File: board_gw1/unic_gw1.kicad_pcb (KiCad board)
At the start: 4 copper layers, 49.5 x 15.2 mm, 109 parts, among them Q1 2N7002, Q10 2N7002, Q11 2N7002, Q12 2N7002, Q13 2N7002, Q14 2N7002, Q15 2N7002, Q16 2N7002, Q17 2N7002, Q18 2N7002, Q19 2N7002, Q2 2N7002, Q20 2N7002, Q21 2N7002, Q22 2N7002, Q23 2N7002, Q24 2N7002, Q25 2N7002, Q26 2N7002, Q27 2N7002, Q28 2N7002, Q29 2N7002, Q3 2N7002, Q30 2N7002, Q31 2N7002, Q32 2N7002, Q33 2N7002, Q34 2N7002, Q35 2N7002, Q36 2N7002, Q37 2N7002, Q38 2N7002, Q39 2N7002, Q4 2N7002, Q40 2N7002, Q5 2N7002, Q6 2N7002, Q7 2N7002, Q8 2N7002, Q9 2N7002, U1 GW1N-LV9QN88C6_I5_, U2 LM3480-3.3, U3 LM3480-5.0, U4 ESP-PSRAM32, U5 AT25SF081-XMHF-X, U6 AP62150Z6, X1 ASE-xxxMHz

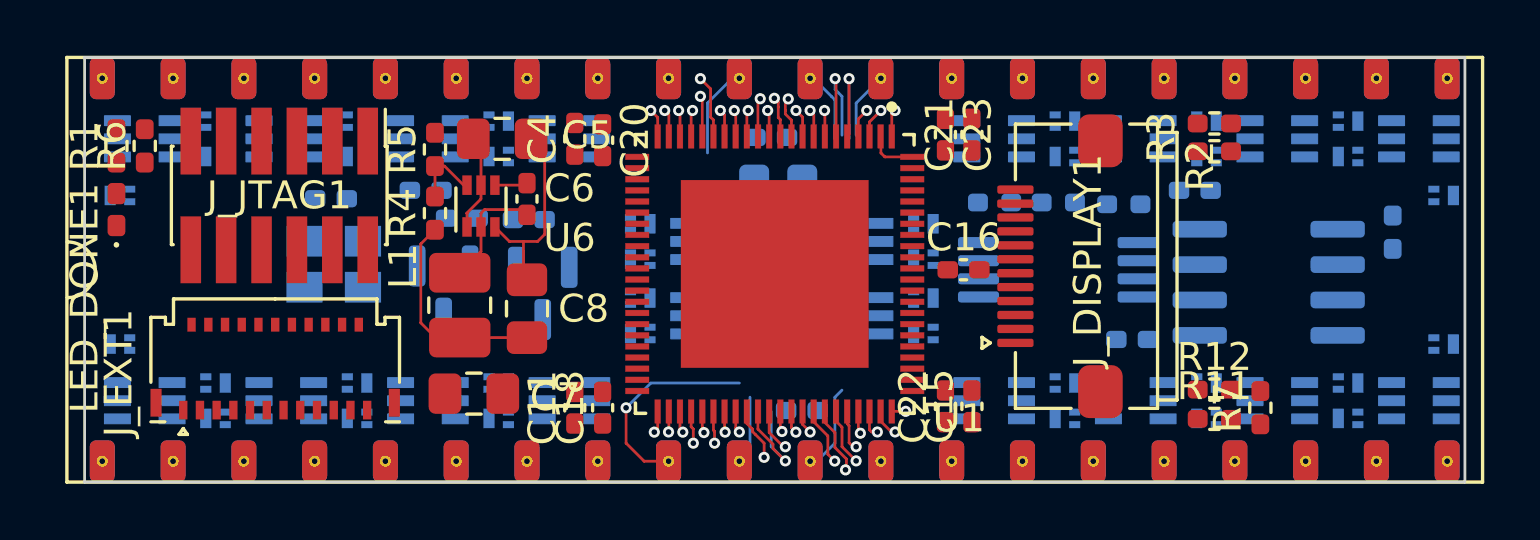
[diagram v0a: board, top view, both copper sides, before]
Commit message: Added extra diodes to shunt ESD path.
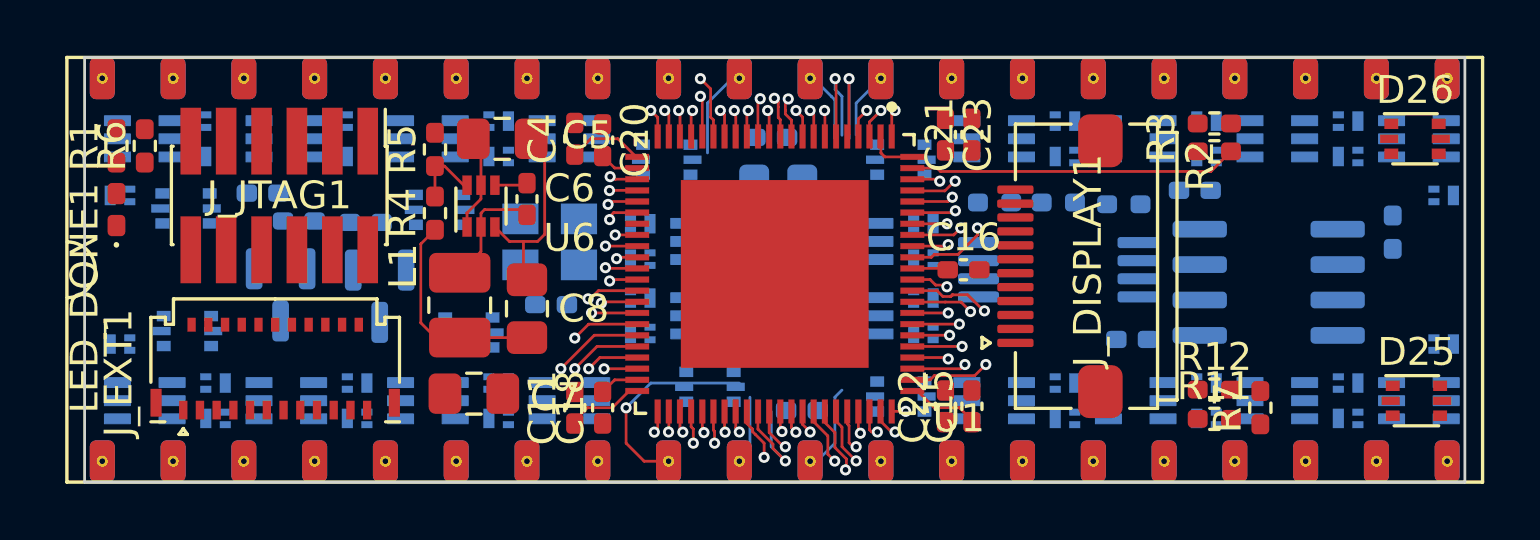
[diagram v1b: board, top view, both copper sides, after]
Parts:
- added D21: BAT54CV, Package_TO_SOT_SMD:SOT-666, B.Cu at (128.2, 97.5)
- added D22: BAT54CV, Package_TO_SOT_SMD:SOT-666, B.Cu at (138.2, 97.5)
- added D23: BAT54CV, Package_TO_SOT_SMD:SOT-666, B.Cu at (146.9, 99.5)
- added D24: BAT54CV, Package_TO_SOT_SMD:SOT-666, B.Cu at (153.8, 99.8)
- added D25: BAT54CV, Package_TO_SOT_SMD:SOT-666, F.Cu at (172.2, 100.0)
- added D26: BAT54CV, Package_TO_SOT_SMD:SOT-666, F.Cu at (172.2, 90.5)
- added D27: BAT54CV, Package_TO_SOT_SMD:SOT-666, B.Cu at (153.8, 91.3)
- added D28: BAT54CV, Package_TO_SOT_SMD:SOT-666, B.Cu at (145.3, 91.3)
- added D29: BAT54CV, Package_TO_SOT_SMD:SOT-666, B.Cu at (137.2, 93.1)
- added D30: BAT54CV, Package_TO_SOT_SMD:SOT-666, B.Cu at (128.1, 93.0)
- moved C17 8.77 mm to (141.2, 96.5)
- moved X1 7.79 mm to (141.2, 94.2)
- moved U3 5.85 mm to (135.1, 96.2)
- moved C1 5.85 mm to (134.6, 93.5)
- moved C2 5.85 mm to (130.8, 92.5)
- moved C3 5.85 mm to (132.2, 93.5)
- moved U2 5.85 mm to (131.5, 96.2)
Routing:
- net Net-(R2-Pad2): track 0.00 -> 11.8 mm
- net +3V3: track 2.77 -> 12.2 mm
- net /PIN2_F: track 0.00 -> 3.24 mm, vias 0 -> 1
- net /PIN20_F: track 0.00 -> 3.01 mm, vias 0 -> 1
- net /PIN22_F: track 0.00 -> 2.92 mm, vias 0 -> 1
- net /PIN12_F: track 0.00 -> 2.87 mm, vias 0 -> 1
- net GND: track 11.7 -> 14.6 mm
- net /PIN3_F: track 0.00 -> 2.64 mm, vias 0 -> 1
- net /PIN1_F: track 0.00 -> 2.45 mm, vias 0 -> 1
- net /PIN19_F: track 0.00 -> 2.23 mm, vias 0 -> 1
- net /PIN13_F: track 0.00 -> 1.95 mm, vias 0 -> 1
- net /PIN4_F: track 0.00 -> 1.91 mm, vias 0 -> 1
- net /IO2A: track 0.00 -> 1.89 mm, vias 0 -> 1
- net /PIN24_F: track 0.00 -> 1.84 mm, vias 0 -> 1
- net /PIN15_F: track 0.00 -> 1.79 mm, vias 0 -> 1
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
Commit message: GW1-based board is fully routed. Cleanup still needed!
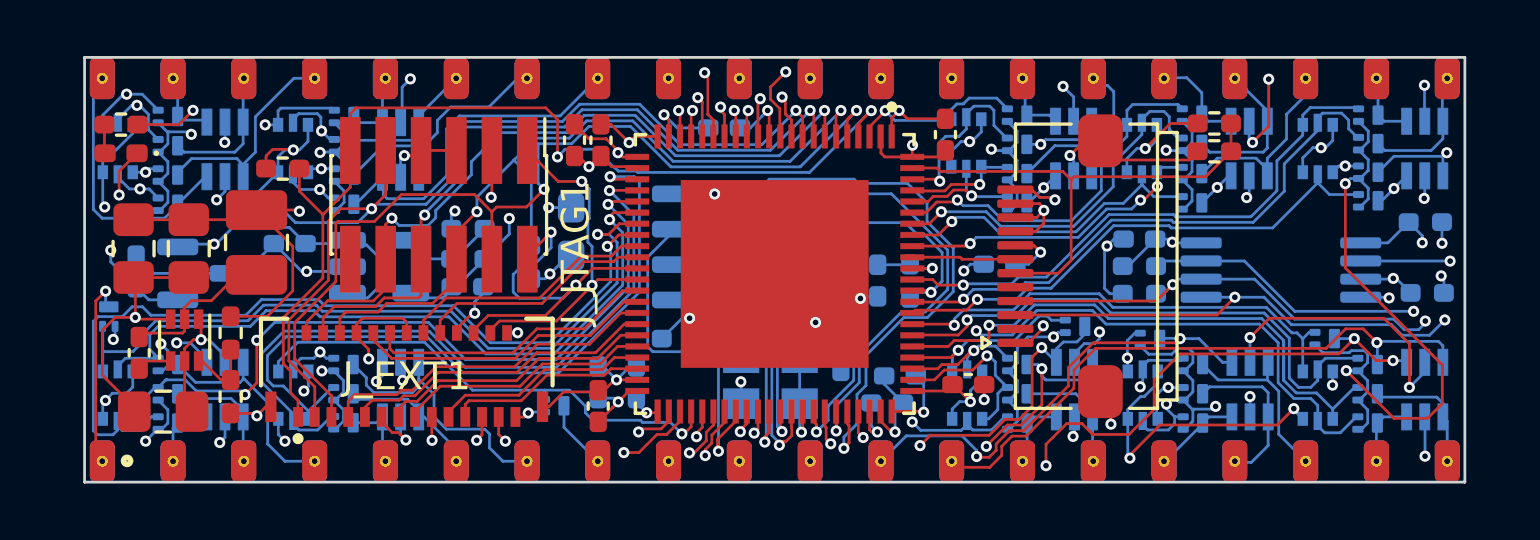
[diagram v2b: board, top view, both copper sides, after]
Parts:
- removed D10, D12, D13, D14, D15, D16, D17, D18, D19, D20: BAT54SDW-7-F, UNIC:SOT65P210X110-6N
- added R14: 4.99k, Resistor_SMD:R_0402_1005Metric_Pad0.72x0.64mm_HandSolder, B.Cu at (138.2, 94.9)
- added R15: 10k, Resistor_SMD:R_0402_1005Metric_Pad0.72x0.64mm_HandSolder, B.Cu at (138.2, 93.8)
- added R16: 10k, Resistor_SMD:R_0402_1005Metric_Pad0.72x0.64mm_HandSolder, F.Cu at (131.6, 91.6)
- C16, C18, C21, C22, D25, D26, R6, R7: moved to B.Cu
- C3: value 0.1u -> 2.2u
- D1, D11, D2, D3, D4, D5, D6, D7, D8, D9: value BAT54SDW-7-F -> BAT54DF
- J_EXT1: value Conn_01x23_MountingPin -> Conn_01x27_MountingPin; footprint UNIC:Molex_502598-2393_2Rows-23Pins-1MP_P0.60mm_Horizontal -> UNIC:Molex_502598-2793_2Rows-23P~0.60mm_Horizontal
- J_JTAG1: footprint Connector_PinHeader_1.27mm:PinHeader_2x06_P1.27mm_Vertical_SMD -> UNIC:PinHeader_2x06_P1.27mm_Vertical_SMD
- Q1, Q10, Q11, Q12, Q13, Q14, Q15, Q16, Q17, Q18, Q19, Q2, Q20, Q21, Q22, Q23, Q24, Q25, Q26, Q27, Q28, Q29, Q3, Q30, Q31, Q32, Q33, Q34, Q35, Q36, Q37, Q38, Q39, Q4, Q40, Q5, Q6, Q7, Q8, Q9: footprint Package_DFN_QFN:Diodes_DFN1006-3 -> UNIC:SOT-883
- R11: value 1k -> 10k; moved to B.Cu
- R12: value DNC -> 10k; moved to B.Cu
- R3: value 1k -> 10k
- U3: value LM3480-5.0 -> AP2202K-ADJ; footprint Package_TO_SOT_SMD:SOT-23 -> Package_TO_SOT_SMD:SOT-23-5
- moved D9 38.8 mm to (129.5, 90.9), turned to -90 degrees
- moved R7 36.7 mm to (130.6, 93.2), turned to 0 degrees
- moved D8 27.9 mm to (135.8, 91.0), turned to -90 degrees
- moved D5 25.7 mm to (172.6, 99.5), turned to -90 degrees
- moved D4 24.4 mm to (166.3, 99.5), turned to -90 degrees
- moved D3 23.2 mm to (160.0, 99.5), turned to -90 degrees
- moved Q11 22.0 mm to (170.5, 89.7)
- moved R12 19.3 mm to (145.8, 97.7), turned to 180 degrees
- moved U4 18.7 mm to (148.3, 94.4), turned to 0 degrees
- moved R13 17.4 mm to (154.1, 95.7), turned to -90 degrees
- moved Q12 17.4 mm to (170.5, 90.7), turned to 0 degrees
- moved C19 16.5 mm to (147.4, 90.2)
- moved Q9 15.6 mm to (160.0, 97.3)
- moved C5 15.6 mm to (127.3, 100.3), turned to 180 degrees
- moved R9 15.5 mm to (172.6, 93.5), turned to 180 degrees
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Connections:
- D1 pad 1: GND -> /PIN1
- D1 pad 3: /PIN1 -> /PIN4
- D1 pad 4: GND -> /PIN3
- D1 pad 5: LINE -> GND
- D11 pad 1: GND -> /PIN22
- D11 pad 4: GND -> /PIN28
- D11 pad 5: LINE -> GND
- D11 pad 6: /PIN22 -> /PIN30
- D2 pad 1: GND -> /PIN8
- D2 pad 3: /PIN3 -> /PIN7
- D2 pad 4: GND -> /PIN6
- D2 pad 5: LINE -> GND
- D2 pad 6: /PIN4 -> /PIN5
- D21 pad 2: /PIN2_F -> /PIN4_F
- D21 pad 5: /PIN4_F -> /PIN2_F
- D22 pad 1: /PIN5_F -> /PIN8_F
- D22 pad 2: /PIN6_F -> /PIN7_F
- D22 pad 4: /PIN7_F -> /PIN6_F
- D22 pad 5: /PIN8_F -> /PIN5_F
- D23 pad 4: /PIN11_F -> /PIN15_F
- D23 pad 5: /PIN12_F -> /PIN14_F
- D24 pad 1: /PIN13_F -> /PIN12_F
- D24 pad 2: /PIN14_F -> /PIN18_F
- D24 pad 4: /PIN15_F -> /PIN17_F
- D25 pad 1: /PIN17_F -> /PIN11_F
- D25 pad 2: /PIN18_F -> /PIN13_F
- D25 pad 4: /PIN19_F -> /PIN20_F
- D25 pad 5: /PIN20_F -> /PIN19_F
- D26 pad 1: /PIN21_F -> /PIN22_F
- D26 pad 2: /PIN22_F -> /PIN21_F
- D26 pad 4: /PIN23_F -> /PIN28_F
- D26 pad 5: /PIN24_F -> /PIN30_F
- D27 pad 2: /PIN26_F -> /PIN24_F
- D27 pad 4: /PIN27_F -> /PIN23_F
- D27 pad 5: /PIN28_F -> /PIN29_F
- D28 pad 1: /PIN29_F -> /PIN27_F
- D28 pad 2: /PIN30_F -> /PIN31_F
- D28 pad 4: /PIN31_F -> /PIN26_F
- D29 pad 1: /PIN33_F -> /PIN36_F
- D29 pad 2: /PIN34_F -> /PIN35_F
- D29 pad 4: /PIN35_F -> /PIN34_F
- D29 pad 5: /PIN36_F -> /PIN33_F
- D3 pad 1: GND -> /PIN9
- D3 pad 3: /PIN5 -> /PIN10
- D3 pad 4: GND -> /PIN15
- D3 pad 5: LINE -> GND
- D3 pad 6: /PIN6 -> /PIN14
- D30 pad 1: /PIN37_F -> /PIN39_F
- D30 pad 4: /PIN39_F -> /PIN37_F
- D4 pad 1: GND -> /PIN12
- D4 pad 3: /PIN7 -> /PIN18
- D4 pad 4: GND -> /PIN17
- D4 pad 5: LINE -> GND
- D4 pad 6: /PIN8 -> /PIN16
- D5 pad 1: GND -> /PIN11
- D5 pad 3: /PIN9 -> /PIN13
- D5 pad 4: GND -> /PIN20
- D5 pad 5: LINE -> GND
- D5 pad 6: /PIN10 -> /PIN19
- D6 pad 1: GND -> /PIN25
- D6 pad 3: /PIN11 -> /PIN24
- D6 pad 4: GND -> /PIN23
- D6 pad 5: LINE -> GND
- D6 pad 6: /PIN12 -> /PIN29
- D7 pad 1: GND -> /PIN27
- D7 pad 3: /PIN13 -> /PIN31
- D7 pad 4: GND -> /PIN26
- D7 pad 5: LINE -> GND
- D7 pad 6: /PIN14 -> /PIN32
- D8 pad 1: GND -> /PIN36
- D8 pad 3: /PIN15 -> /PIN35
- D8 pad 4: GND -> /PIN34
- D8 pad 5: LINE -> GND
- D8 pad 6: /PIN16 -> /PIN33
- D9 pad 1: GND -> /PIN39
- D9 pad 3: /PIN17 -> /PIN38
- D9 pad 4: GND -> /PIN37
- D9 pad 5: LINE -> GND
- D9 pad 6: /PIN18 -> /PIN40
- J_EXT1 pad 1: GND -> /JTAG_SEL_N
- J_EXT1 pad 10: GND -> /IO2A
- J_EXT1 pad 11: /IO4A -> GND
- J_EXT1 pad 12: /IO4B -> /IO2B
- J_EXT1 pad 13: GND -> /IO3A
- J_EXT1 pad 14: /IO5A -> GND
- J_EXT1 pad 15: /IO5B -> /IO3B
- J_EXT1 pad 16: GND -> /IO4A
- J_EXT1 pad 17: /IO6A -> GND
- J_EXT1 pad 18: /IO6B -> /IO4B
- J_EXT1 pad 19: /RECONFIG_N -> /IO5A
- J_EXT1 pad 2: /IO1A -> /JTAG_TDI
- J_EXT1 pad 20: /JTAG_SEL_N -> GND
- J_EXT1 pad 21: +5V -> /IO5B
- J_EXT1 pad 22: +3V3 -> /IO6A
- J_EXT1 pad 23: +3V3 -> GND
- J_EXT1 pad 3: /IO1B -> /RECONFIG_N
- J_EXT1 pad 4: GND -> /JTAG_TDO
- J_EXT1 pad 5: /IO2A -> /JTAG_TMS
- J_EXT1 pad 6: /IO2B -> /JTAG_TCK
- J_EXT1 pad 7: GND -> /IO1A
- J_EXT1 pad 8: /IO3A -> GND
- J_EXT1 pad 9: /IO3B -> /IO1B
- J_JTAG1 pad 1: /SER_RXD -> /IO6B
- J_JTAG1 pad 10: /JTAG_TDO -> /JTAG_TDI
- J_JTAG1 pad 12: /JTAG_RST -> unconnected-(J_JTAG1-Pad12)
- J_JTAG1 pad 2: /SER_TXD -> /IO6A
- Q11 pad 2: /PIN11_F -> /PIN22_F
- Q11 pad 3: /PIN11 -> /PIN22
- Q12 pad 2: /PIN12_F -> /PIN21_F
- Q12 pad 3: /PIN12 -> /PIN21
- Q13 pad 2: /PIN13_F -> /PIN15_F
- Q13 pad 3: /PIN13 -> /PIN15
- Q15 pad 2: /PIN15_F -> /PIN12_F
- Q15 pad 3: /PIN15 -> /PIN12
- Q16 pad 2: /PIN16_F -> /PIN18_F
- Q16 pad 3: /PIN16 -> /PIN18
- Q18 pad 2: /PIN18_F -> /PIN16_F
- Q18 pad 3: /PIN18 -> /PIN16
- Q19 pad 2: /PIN19_F -> /PIN11_F
- Q19 pad 3: /PIN19 -> /PIN11
- Q2 pad 2: /PIN2_F -> /PIN4_F
- Q2 pad 3: /PIN2 -> /PIN4
- Q20 pad 2: /PIN20_F -> /PIN13_F
- Q20 pad 3: /PIN20 -> /PIN13
- Q21 pad 2: /PIN21_F -> /PIN20_F
- Q21 pad 3: /PIN21 -> /PIN20
- Q22 pad 2: /PIN22_F -> /PIN19_F
- Q22 pad 3: /PIN22 -> /PIN19
- Q23 pad 2: /PIN23_F -> /PIN25_F
- Q23 pad 3: /PIN23 -> /PIN25
- Q25 pad 2: /PIN25_F -> /PIN28_F
- Q25 pad 3: /PIN25 -> /PIN28
- Q26 pad 2: /PIN26_F -> /PIN30_F
- Q26 pad 3: /PIN26 -> /PIN30
- Q27 pad 2: /PIN27_F -> /PIN23_F
- Q27 pad 3: /PIN27 -> /PIN23
- Q28 pad 2: /PIN28_F -> /PIN29_F
- Q28 pad 3: /PIN28 -> /PIN29
- Q29 pad 2: /PIN29_F -> /PIN27_F
- Q29 pad 3: /PIN29 -> /PIN27
- Q30 pad 2: /PIN30_F -> /PIN31_F
- Q30 pad 3: /PIN30 -> /PIN31
- Q31 pad 2: /PIN31_F -> /PIN26_F
- Q31 pad 3: /PIN31 -> /PIN26
- Q33 pad 2: /PIN33_F -> /PIN36_F
- Q33 pad 3: /PIN33 -> /PIN36
- Q34 pad 2: /PIN34_F -> /PIN35_F
- Q34 pad 3: /PIN34 -> /PIN35
- Q35 pad 2: /PIN35_F -> /PIN34_F
- Q35 pad 3: /PIN35 -> /PIN34
- Q36 pad 2: /PIN36_F -> /PIN33_F
- Q36 pad 3: /PIN36 -> /PIN33
- Q37 pad 2: /PIN37_F -> /PIN39_F
- Q37 pad 3: /PIN37 -> /PIN39
- Q39 pad 2: /PIN39_F -> /PIN37_F
- Q39 pad 3: /PIN39 -> /PIN37
- Q4 pad 2: /PIN4_F -> /PIN2_F
- Q4 pad 3: /PIN4 -> /PIN2
- Q5 pad 2: /PIN5_F -> /PIN8_F
- Q5 pad 3: /PIN5 -> /PIN8
- Q6 pad 2: /PIN6_F -> /PIN7_F
- Q6 pad 3: /PIN6 -> /PIN7
- Q7 pad 2: /PIN7_F -> /PIN6_F
- Q7 pad 3: /PIN7 -> /PIN6
- Q8 pad 2: /PIN8_F -> /PIN5_F
- Q8 pad 3: /PIN8 -> /PIN5
- R12 pad 1: /PSRAM_CS_N -> Net-(R12-Pad1)
- R2 pad 2: Net-(R2-Pad2) -> /LCD_RST_N
- R3 pad 1: Net-(R2-Pad2) -> /LCD_RST_N
- R7 pad 2: /RECONIFG_N -> /RECONFIG_N
- U1 pad 11: /PIN34_F -> /PIN28_F
- U1 pad 14: /PIN32_F -> /PIN34_F
- U1 pad 15: /PIN31_F -> /PIN35_F
- U1 pad 16: /PIN35_F -> /PIN36_F
- U1 pad 17: /PIN36_F -> /PIN39_F
- U1 pad 18: /PIN37_F -> /PIN38_F
- U1 pad 19: /PIN38_F -> /PIN40_F
- U1 pad 20: /PIN39_F -> /PIN37_F
- U1 pad 25: /IO6B -> /PIN6_F
- U1 pad 26: /IO6A -> /PIN5_F
- U1 pad 27: /PIN40_F -> /PIN3_F
- U1 pad 28: /IO5B -> /PIN4_F
- U1 pad 29: /IO5A -> /PIN1_F
- U1 pad 3: /PIN30_F -> /PIN27_F
- U1 pad 30: /IO4B -> /PIN2_F
- U1 pad 32: /IO3B -> /IO4B
- U1 pad 33: /IO3A -> /IO6A
- U1 pad 34: /IO2B -> /IO6B
- U1 pad 35: /IO2A -> /IO2B
- U1 pad 36: /IO1B -> /IO2A
- U1 pad 38: /PIN1_F -> /IO1B
- U1 pad 39: /PIN2_F -> /IO3A
- U1 pad 40: /PIN3_F -> /IO3B
- U1 pad 41: /PIN4_F -> /IO5A
- U1 pad 42: /PIN5_F -> /IO5B
- U1 pad 47: /PIN6_F -> /PIN7_F
- U1 pad 48: /PIN7_F -> /PIN8_F
- U1 pad 49: /PIN8_F -> /PIN19_F
- U1 pad 50: /PIN9_F -> /PIN12_F
- U1 pad 51: /PIN10_F -> /PIN18_F
- U1 pad 53: /LCD_RST_N -> /PIN17_F
- U1 pad 54: /LCD_CS_N -> /PIN16_F
- U1 pad 57: /PSRAM_CS_N -> Net-(R12-Pad1)
- U1 pad 63: /PIN11_F -> /PIN14_F
- U1 pad 68: /PIN12_F -> /PIN15_F
- U1 pad 69: /PIN13_F -> /PIN10_F
- U1 pad 70: /PIN14_F -> /PIN9_F
- U1 pad 71: /PIN15_F -> /PIN20_F
- U1 pad 72: /PIN16_F -> /PIN13_F
- U1 pad 73: /PIN17_F -> /PIN11_F
- U1 pad 74: /PIN18_F -> /PIN30_F
- U1 pad 75: /PIN19_F -> /PIN21_F
- U1 pad 76: /PIN20_F -> /PSRAM_CS_N
- U1 pad 77: /PIN21_F -> /PIN22_F
- U1 pad 79: /PIN22_F -> /LCD_CS_N
- U1 pad 81: /PIN24_F -> /PIN29_F
- U1 pad 82: /PIN25_F -> /PIN24_F
- U1 pad 83: /PIN26_F -> /PIN25_F
- U1 pad 84: /PIN27_F -> /PIN32_F
- U1 pad 85: /PIN28_F -> /PIN26_F
- U1 pad 86: /PIN29_F -> /PIN31_F
- U1 pad 87: Net-(R2-Pad2) -> /LCD_RST_N
- U1 pad 9: /RECONIFG_N -> /RECONFIG_N
- U3 pad 1: +5V -> LINE
- U3 pad 2: LINE -> GND
- U3 pad 3: GND -> LINE
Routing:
- net +3V3: track 12.2 -> 222.4 mm, vias 3 -> 28
- net GND: track 14.6 -> 221.9 mm, vias 3 -> 38
- net +5V: track 0.00 -> 186.6 mm, vias 0 -> 14
- net LINE: track 3.49 -> 111.9 mm, vias 0 -> 12
- net /SPI_MOSI_IO0: track 2.07 -> 59.4 mm, vias 1 -> 3
- net /SPI_MISO_IO1: track 1.46 -> 56.8 mm, vias 1 -> 2
- net +1V2: track 10.9 -> 63.8 mm, vias 4 -> 5
- net /SPI_CLK: track 2.09 -> 52.9 mm, vias 1 -> 3
- net /SPI_IO3: track 0.74 -> 46.7 mm, vias 1 -> 2
- net /SPI_IO2: track 1.55 -> 46.9 mm, vias 1 -> 2
- net /RECONFIG_N: track 0.00 -> 35.9 mm, vias 0 -> 2
- net /JTAG_SEL_N: track 1.06 -> 36.9 mm, vias 1 -> 2
- net /FLASH_CS_N: track 2.43 -> 35.1 mm, vias 1 -> 2
- net /JTAG_TMS: track 4.26 -> 34.2 mm, vias 1 -> 2
- net /PIN19_F: track 2.23 -> 29.8 mm, vias 1 -> 2
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
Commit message: Small fixes to board file
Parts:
- moved R12 0.31 mm to (145.5, 97.7)
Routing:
- net /CLK1: track 4.81 -> 6.51 mm
- net GND: track 221.9 -> 223.1 mm

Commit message: Board more or less done.
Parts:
- moved C7 0.50 mm to (126.2, 94.0)
- moved C1 0.32 mm to (131.8, 94.6)
- moved C8 0.20 mm to (128.2, 94.3)
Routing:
- net +5V: track 186.6 -> 149.4 mm, vias 14 -> 15
- net GND: track 223.1 -> 215.5 mm, vias 38 -> 37
- net /PIN29: track 15.1 -> 20.4 mm, vias 1 -> 2
- net /PIN39: track 2.05 -> 4.47 mm
- net /PIN30: track 24.3 -> 25.7 mm
- net /PIN38_F: track 24.5 -> 25.7 mm
- net +3V3: track 222.4 -> 223.6 mm, vias 28 -> 29
- net /JTAG_TDO: track 25.9 -> 24.8 mm
- net /RECONFIG_N: track 35.9 -> 34.7 mm
- net /JTAG_TCK: track 26.7 -> 25.7 mm
- net /PIN8: track 12.4 -> 13.5 mm
- net /PIN6_F: track 25.8 -> 25.0 mm
- net /JTAG_SEL_N: track 36.9 -> 37.6 mm
- net /PIN3_F: track 26.7 -> 27.4 mm
- net /PIN34: track 8.45 -> 9.15 mm
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- added copper zone on In2.Cu, net +1V2
- added copper zone on In1.Cu, net +3V3
- added copper zone on In2.Cu, net +3V3
- added copper zone on In1.Cu, net +5V
- added copper zone on In2.Cu, net +5V
- added copper zone on In1.Cu, net GND
- added copper zone on F.Cu, net LINE
- added copper zone on In1.Cu, net LINE
- added copper zone on In2.Cu, net LINE

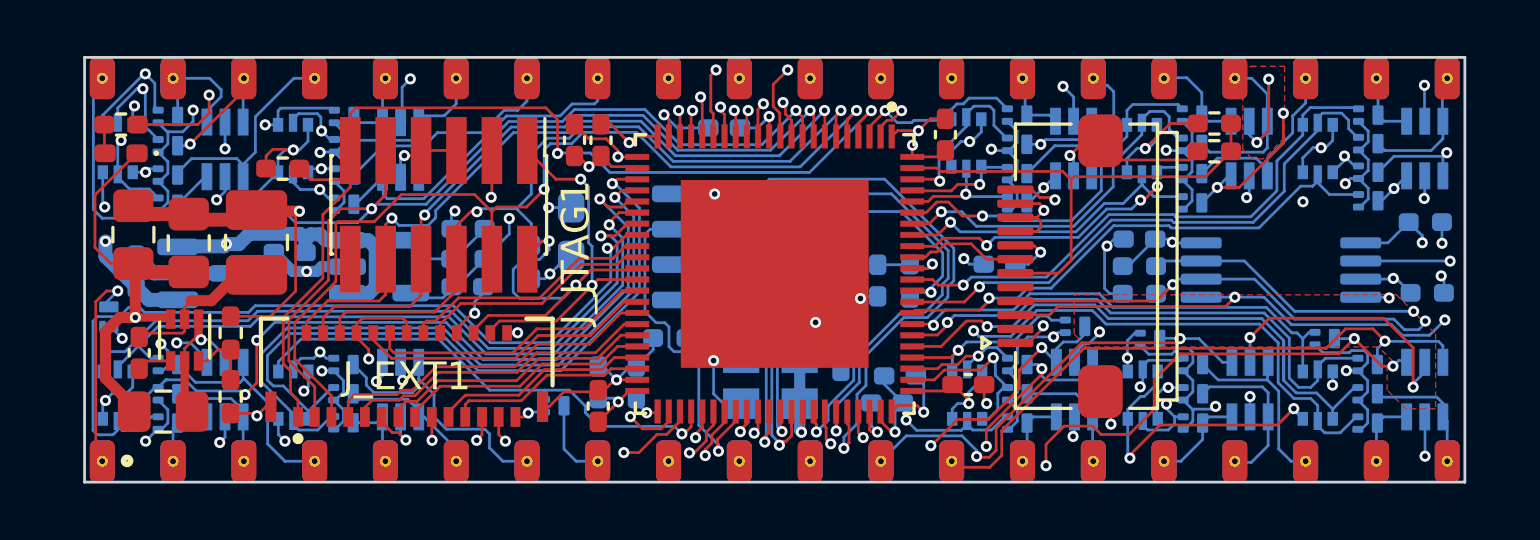
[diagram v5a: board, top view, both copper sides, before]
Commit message: Updated FLASH part to package that's actually available.
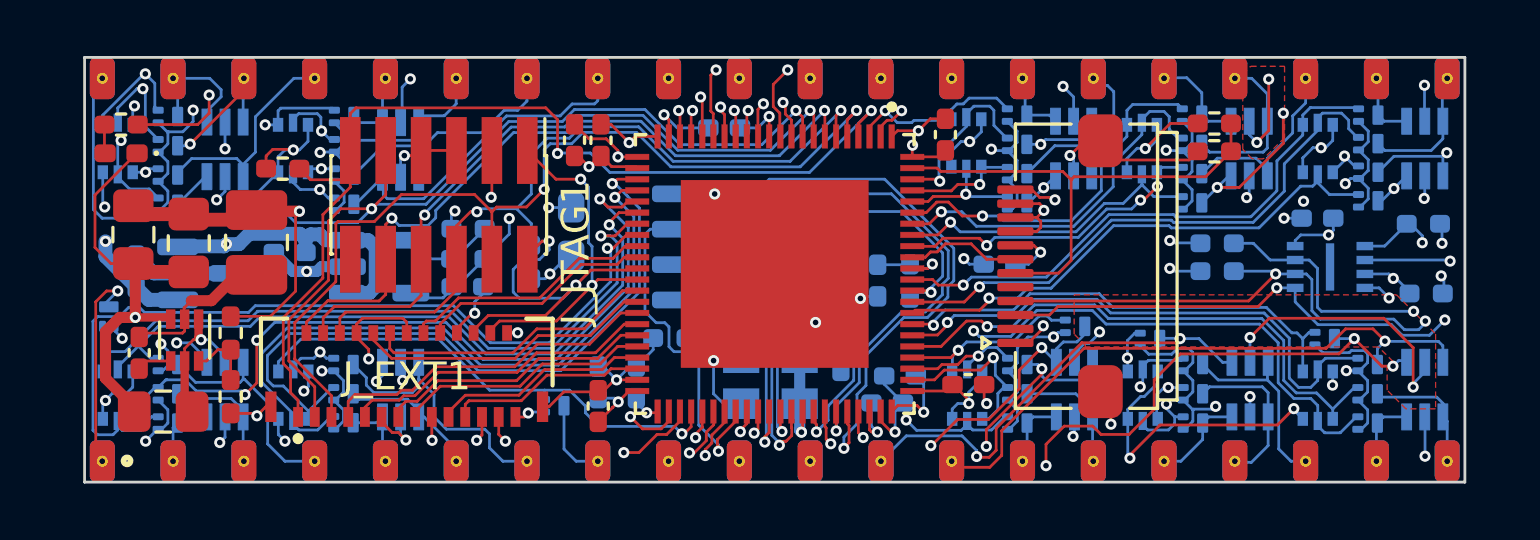
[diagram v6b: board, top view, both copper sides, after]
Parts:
- removed U5: AT25SF081-XMHF-X, Package_SO:TSSOP-8_4.4x3mm_P0.65mm
- added U7: W25Q16JVUXIQ, UNIC:W25Q16JVUXIQ_TR, B.Cu at (169.2, 95.2)
- R2: value DNC -> 1k
- moved C14 6.43 mm to (168.7, 93.4)
- moved R10 2.91 mm to (165.1, 94.3)
- moved R11 2.91 mm to (165.1, 95.3)
- moved R9 2.56 mm to (172.6, 96.1)
- moved R8 2.48 mm to (172.5, 93.6)
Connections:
- R8 pad 2: /SPI_IO2 -> /FLASH_CS_N
- R9 pad 2: /FLASH_CS_N -> /SPI_IO2
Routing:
- net GND: track 215.5 -> 212.3 mm, vias 37 -> 38
- net /SPI_CLK: track 53.3 -> 55.2 mm
- net /SPI_IO3: track 46.8 -> 45.3 mm
- net /PIN20_F: track 21.1 -> 19.7 mm
- net /JTAG_SEL_N: track 37.6 -> 36.6 mm
- net +1V2: track 64.0 -> 63.3 mm
- net LINE: track 112.6 -> 111.9 mm
- net /SPI_MOSI_IO0: track 59.4 -> 58.7 mm
- net +3V3: track 223.6 -> 223.7 mm, vias 29 -> 30

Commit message: Updated footprints for LCD connector and PSRAM
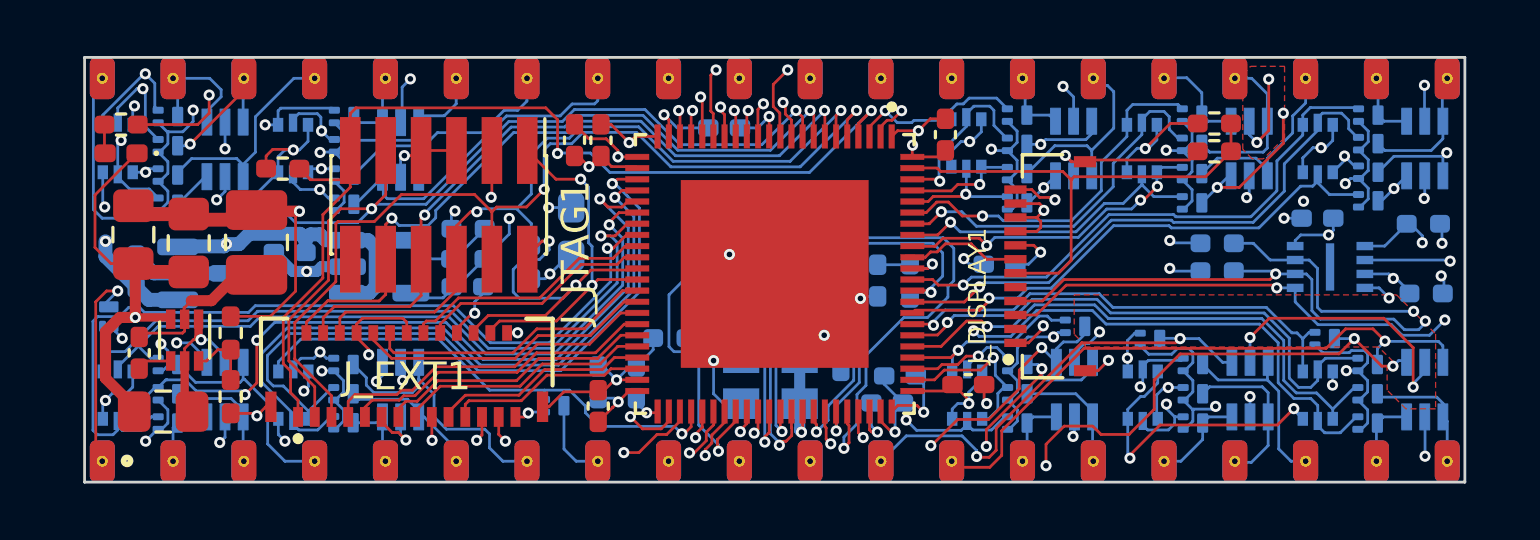
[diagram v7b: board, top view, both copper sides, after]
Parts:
- J_DISPLAY1: footprint UNIC:CF31121D0R0-05-NH -> UNIC:HRS_FH19C-12S-0.5SH_05_
- U4: value ESP-PSRAM32 -> APS6404L-3SQR-ZR; footprint Package_SO:SOIC-8_3.9x4.9mm_P1.27mm -> UNIC:W25Q16JVUXIQ_TR
- moved U4 1.71 mm to (149.6, 95.5)
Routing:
- net +3V3: track 223.7 -> 75.2 mm
- net GND: track 212.3 -> 85.3 mm
- net +5V: track 149.4 -> 54.3 mm
- net LINE: track 111.9 -> 47.5 mm
- net +1V2: track 63.3 -> 40.0 mm
- net /SPI_MOSI_IO0: track 58.7 -> 52.3 mm
- net /SPI_MISO_IO1: track 56.4 -> 52.4 mm
- net /PSRAM_CS_N: track 15.2 -> 11.4 mm
- net /SPI_CLK: track 55.2 -> 53.4 mm
- net /SPI_IO3: track 45.3 -> 44.3 mm
- net /SPI_IO2: track 47.1 -> 46.5 mm
